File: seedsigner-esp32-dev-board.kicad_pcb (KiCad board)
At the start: 2 copper layers, 71.1 x 78.7 mm, 5 parts, among them J1 Conn_01x05, U1 ESP32-S2-SAOLA-1M, U2 OV_CAMERA, U3 RASPBERRY_PI_3_MODEL_B+

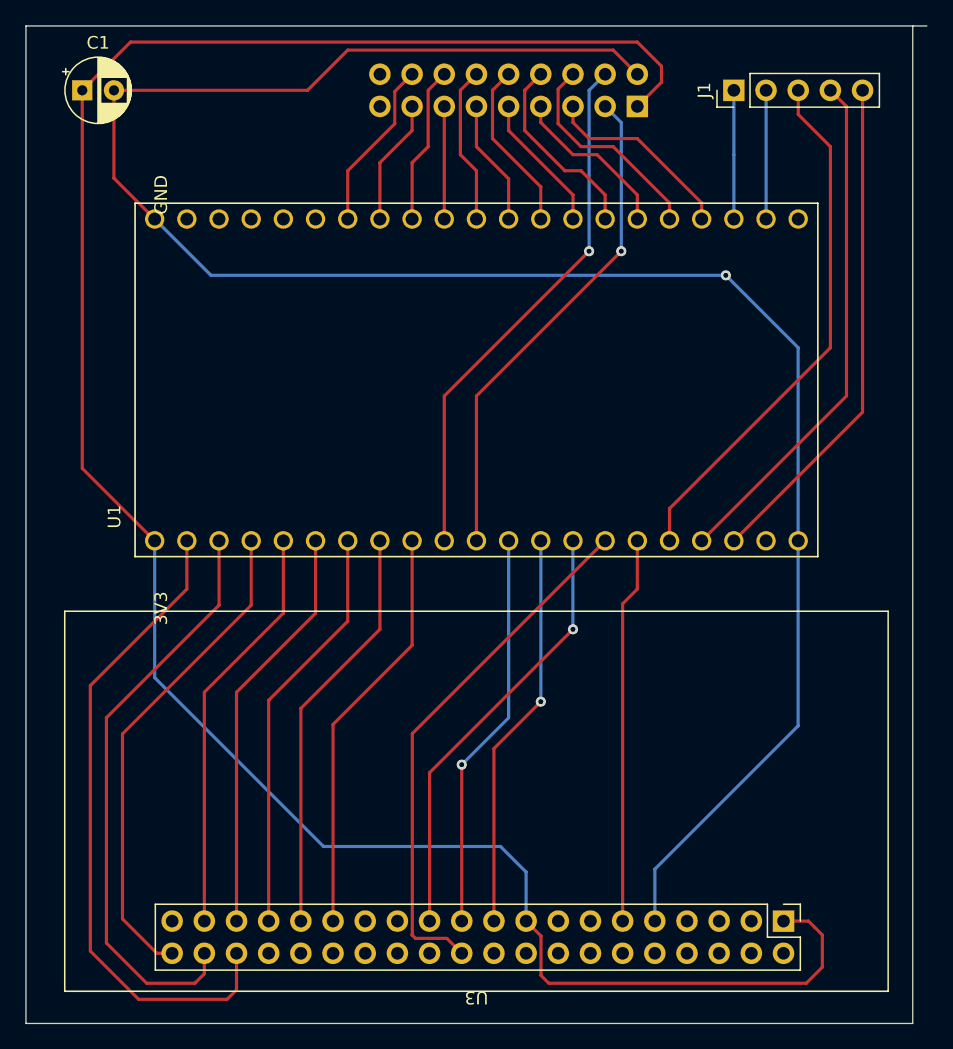
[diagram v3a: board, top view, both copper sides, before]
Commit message: fix small wiring issue, add mounting hole for lcd, add silkscreen
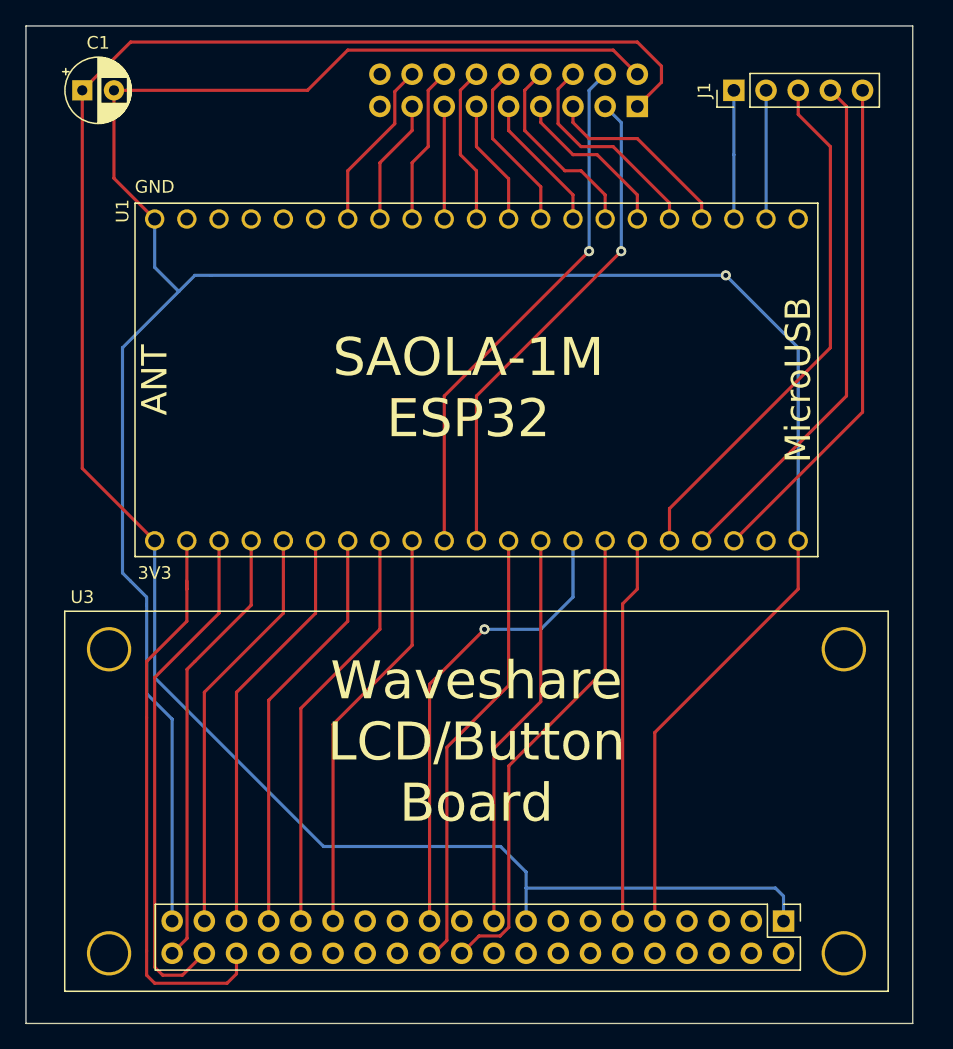
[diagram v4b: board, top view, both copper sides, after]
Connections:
- U3 pad 21: /SPI_CS -> unconnected-(U3-Pad21)
- U3 pad 24: unconnected-(U3-Pad24) -> /SPI_CS
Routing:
- net GND: track 159.9 -> 216.3 mm
- net +3.3V: track 174.1 -> 162.9 mm
- net /KEY3: track 51.9 -> 45.5 mm
- net /KEY2: track 46.4 -> 40.7 mm
- net /KEY1: track 39.1 -> 35.1 mm
- net /SPI_CS: track 31.6 -> 35.3 mm, vias 1 -> 0
- net /DC: track 41.9 -> 38.2 mm
- net /SPI_SCLK: track 34.7 -> 37.3 mm
- net /SPI_MOSI: vias 1 -> 0
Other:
- board size 71.1 x 78.7 mm -> 70 x 78.7 mm
- board text added: "ANT"
- board text added: "MicroUSB"
- board text added: "OV2640 Camera"
- board text added: "SAOLA-1M ESP32"
- board text added: "Waveshare LCD/Button Board"

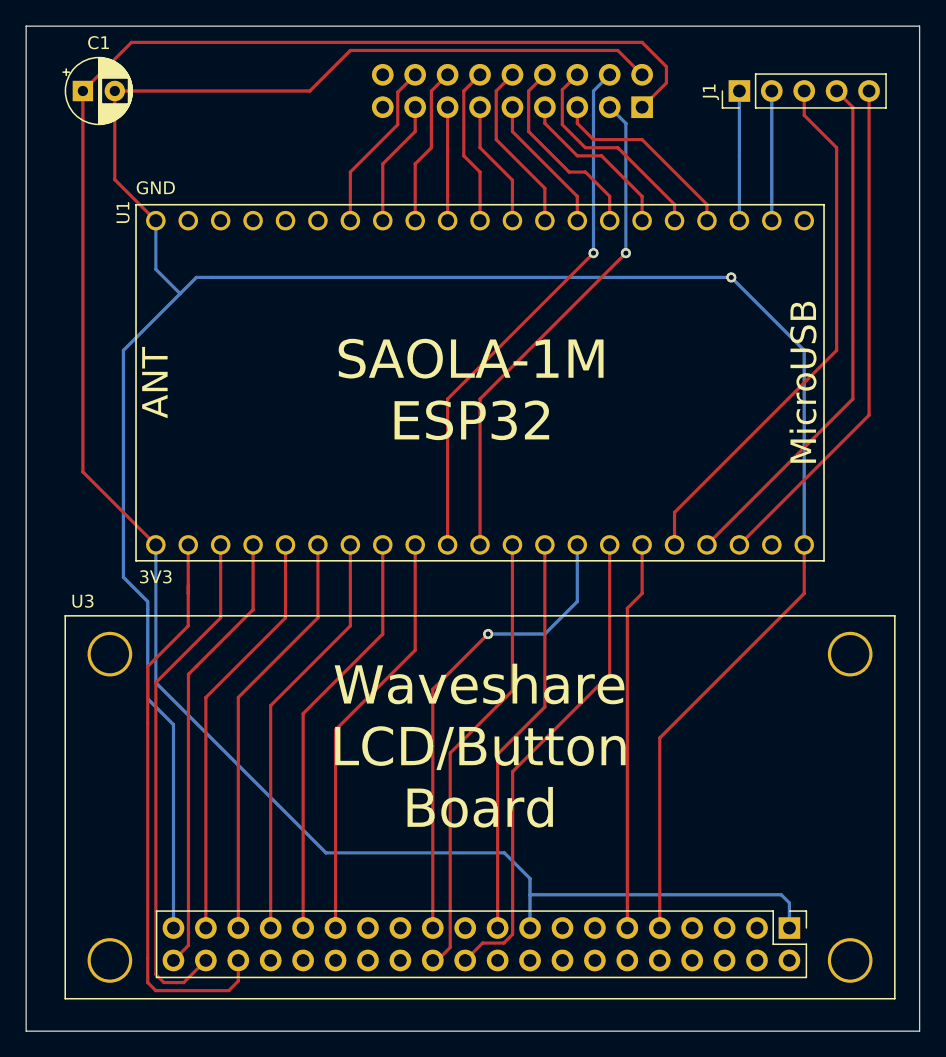
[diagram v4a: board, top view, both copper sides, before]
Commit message: add holes and seedsigner logo
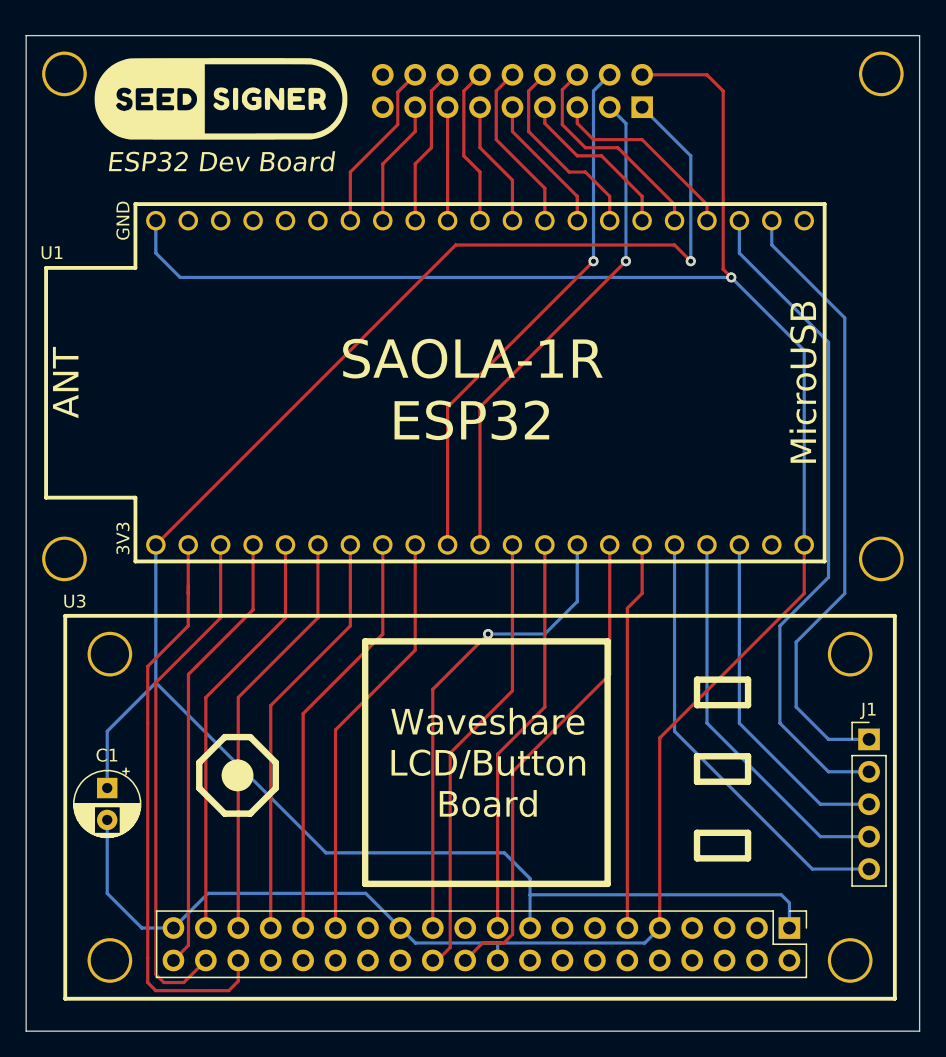
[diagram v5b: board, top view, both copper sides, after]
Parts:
- added H1: MountingHole, SeedSigner:MOUNT_HOLE_3MM, F.Cu at (67.0, -37.0)
- added H2: MountingHole, SeedSigner:MOUNT_HOLE_3MM, F.Cu at (3.00, -37.0)
- added H3: MountingHole, SeedSigner:MOUNT_HOLE_3MM, F.Cu at (67.0, -75.0)
- added H4: MountingHole, SeedSigner:MOUNT_HOLE_3MM, F.Cu at (3.00, -75.0)
- added LOGO1: SS_LOGO, SeedSigner:seedsigner-logo-small, F.Cu at (15.2, -73.0)
- moved C1 54.6 mm to (6.35, -19.1), turned to -90 degrees
- moved J1 51.8 mm to (66.0, -22.9), turned to 0 degrees
- moved U3 15.0 mm to (35.6, -17.5)
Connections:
- U1 pad 15: /XTRA3 -> /XTRA5
- U1 pad 17: /XTRA5 -> /XTRA3
- U1 pad 19: /XTRA2 -> /XTRA1
- U1 pad 20: /XTRA1 -> /XTRA2
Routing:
- net /XTRA2: track 10.2 -> 52.4 mm
- net /XTRA1: track 10.2 -> 48.8 mm
- net GND: track 216.3 -> 183.0 mm
- net /XTRA3: track 41.9 -> 26.8 mm
- net +3.3V: track 162.9 -> 148.5 mm, vias 0 -> 1
- net /XTRA4: track 40.8 -> 30.4 mm
- net /XTRA5: track 39.8 -> 34.3 mm
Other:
- board size 70 x 78.7 mm -> 70 x 78 mm
- board text added: "ESP32 Dev Board"
- board text added: "SAOLA-1R ESP32"
- board text removed: "SAOLA-1M ESP32"

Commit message: cleanup and add header for DE2120
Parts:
- added J2: Conn_01x08, Connector_PinSocket_2.00mm:PinSocket_1x08_P2.00mm_Vertical, B.Cu at (65.5, -24.2)
- J1: value Conn_01x05 -> Conn_01x06; footprint Connector_PinHeader_2.54mm:PinHeader_1x05_P2.54mm_Vertical -> Connector_PinHeader_2.54mm:PinHeader_1x06_P2.54mm_Vertical; moved to B.Cu
- moved J1 68.9 mm to (21.8, -75.7), turned to 90 degrees
- moved LOGO1 2.47 mm to (14.7, -70.6)
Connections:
- J1 pad 1: /XTRA1 -> GND
- J1 pad 2: /XTRA2 -> /TX
- J1 pad 3: /XTRA3 -> /RX
- J1 pad 4: /XTRA4 -> +3.3V
- J1 pad 5: /XTRA5 -> /IO_TRIG
- U1 pad 45: unconnected-(U1-Pad45) -> /IO_TRIG
- U1 pad 46: unconnected-(U1-Pad46) -> /IO_IN
- U1 pad RX: unconnected-(U1-PadRX) -> /RX
- U1 pad TX: unconnected-(U1-PadTX) -> /TX
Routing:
- net +3.3V: track 148.5 -> 181.1 mm
- net GND: track 183.0 -> 214.5 mm
- net +5V: track 0.00 -> 21.7 mm, vias 0 -> 1
- net /IO_TRIG: track 0.00 -> 14.7 mm
- net /IO_IN: track 0.00 -> 14.7 mm
- net /RX: track 0.00 -> 13.7 mm
- net /TX: track 0.00 -> 13.7 mm
- net /XTRA1: track 48.8 -> 50.5 mm
- net /XTRA4: track 30.4 -> 31.9 mm
- net /XTRA2: track 52.4 -> 53.9 mm
- net /XTRA5: track 34.3 -> 35.3 mm
- net /XTRA3: track 26.8 -> 27.6 mm
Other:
- board text added: "3.3V"
- board text added: "5V"
- board text added: "DE2120 Scanner"
- board text added: "Dev Board"
- board text added: "EXPANSION"
- board text added: "GND"
- board text added: "P15"
- board text added: "P16"
- board text added: "P17"
- board text added: "P19"
- board text added: "P20"
- board text added: "RX"
- board text added: "SAOLA-1R"
- board text added: "STAT"
- board text added: "TRIG"
- board text added: "TX"
- board text added: "Waveshare LCD HAT"
- board text removed: "ESP32 Dev Board"
- board text removed: "SAOLA-1R ESP32"
- board text removed: "Waveshare LCD/Button Board"

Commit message: small silkscreen adjustments
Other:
- board text added: "15"
- board text added: "16"
- board text added: "17"
- board text added: "19"
- board text added: "20"
- board text removed: "DE2120 Scanner"
- board text removed: "P15"
- board text removed: "P16"
- board text removed: "P17"
- board text removed: "P19"
- board text removed: "P20"
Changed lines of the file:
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@@
     (property "Sheetname" "")
     (attr through_hole)
-    (fp_text reference "J1" (at 0 2.54 90) (layer "B.SilkS")
+    (fp_text reference "J1" (at 0 -15.24 270) (layer "B.SilkS")
       (effects (font (size 1 1) (thickness 0.15)) (justify mirror))
     )
@@
     (property "Sheetname" "")
     (attr through_hole)
-    (fp_text reference "J2" (at 0 2.5) (layer "B.SilkS")
+    (fp_text reference "J2" (at 0 2.192) (layer "B.SilkS")
       (effects (font (size 1 1) (thickness 0.15)) (justify mirror))
     )
@@
   (gr_line (start 0 -78) (end 0 0) (layer "Edge.Cuts") (width 0.1))
   (gr_line (start 70 0) (end 70 -78) (layer "Edge.Cuts") (width 0.1))
-  (gr_text "RX" (at 16.764 -73.66) (layer "B.SilkS")
-    (effects (font (size 0.7 0.7) (thickness 0.125)) (justify mirror))
-  )
-  (gr_text "3.3V" (at 67.31 -9.144 90) (layer "B.SilkS")
+  (gr_text "RX" (at 16.764 -73.406 270) (layer "B.SilkS")
+    (effects (font (size 0.7 0.7) (thickness 0.125)) (justify mirror))
+  )
+  (gr_text "3.3V" (at 68.072 -10.16) (layer "B.SilkS")
     (effects (font (size 0.7 0.7) (thickness 0.125)) (justify mirror))
   )
@@
     (effects (font (size 1.5 1.5) (thickness 0.3)) (justify mirror))
   )
-  (gr_text "GND" (at 67.31 -24.638 90) (layer "B.SilkS")
-    (effects (font (size 0.7 0.7) (thickness 0.125)) (justify mirror))
-  )
-  (gr_text "P16" (at 67.31 -13.97 90) (layer "B.SilkS")
+  (gr_text "GND" (at 67.818 -24.13) (layer "B.SilkS")
+    (effects (font (size 0.7 0.7) (thickness 0.125)) (justify mirror))
+  )
+  (gr_text "16" (at 67.564 -13.97) (layer "B.SilkS")
     (effects (font (size 0.7 0.7) (thickness 0.125)) (justify mirror))
   )
@@
     (effects (font (size 2 2) (thickness 0.3)) (justify mirror))
   )
-  (gr_text "GND" (at 21.844 -73.66) (layer "B.SilkS")
-    (effects (font (size 0.7 0.7) (thickness 0.125)) (justify mirror))
-  )
-  (gr_text "P19" (at 67.31 -20.828 90) (layer "B.SilkS")
-    (effects (font (size 0.7 0.7) (thickness 0.125)) (justify mirror))
-  )
-  (gr_text "STAT" (at 8.89 -73.66) (layer "B.SilkS")
-    (effects (font (size 0.7 0.7) (thickness 0.125)) (justify mirror))
-  )
-  (gr_text "5V" (at 67.31 -22.606 90) (layer "B.SilkS")
-    (effects (font (size 0.7 0.7) (thickness 0.125)) (justify mirror))
-  )
-  (gr_text "DE2120\nScanner" (at 15.24 -70.104) (layer "B.SilkS")
-    (effects (font (size 2 2) (thickness 0.3)) (justify mirror))
-  )
-  (gr_text "P17" (at 67.31 -16.256 90) (layer "B.SilkS")
-    (effects (font (size 0.7 0.7) (thickness 0.125)) (justify mirror))
-  )
-  (gr_text "P20" (at 67.31 -18.542 90) (layer "B.SilkS")
-    (effects (font (size 0.7 0.7) (thickness 0.125)) (justify mirror))
-  )
-  (gr_text "3.3V" (at 14.478 -73.66) (layer "B.SilkS")
-    (effects (font (size 0.7 0.7) (thickness 0.125)) (justify mirror))
-  )
-  (gr_text "TRIG" (at 11.684 -73.66) (layer "B.SilkS")
-    (effects (font (size 0.7 0.7) (thickness 0.125)) (justify mirror))
-  )
-  (gr_text "P15" (at 67.31 -11.684 90) (layer "B.SilkS")
-    (effects (font (size 0.7 0.7) (thickness 0.125)) (justify mirror))
-  )
-  (gr_text "TX" (at 19.304 -73.66) (layer "B.SilkS")
-    (effects (font (size 0.7 0.7) (thickness 0.125)) (justify mirror))
-  )
+  (gr_text "EXPANSION" (at 14.732 -70.612) (layer "B.SilkS")
+    (effects (font (size 1.5 1.5) (thickness 0.3)) (justify mirror))
+  )
+  (gr_text "GND" (at 21.844 -72.898 270) (layer "B.SilkS")
+    (effects (font (size 0.7 0.7) (thickness 0.125)) (justify mirror))
+  )
+  (gr_text "19" (at 67.564 -20.32) (layer "B.SilkS")
+    (effects (font (size 0.7 0.7) (thickness 0.125)) (justify mirror))
+  )
+  (gr_text "STAT" (at 9.144 -72.898 270) (layer "B.SilkS")
+    (effects (font (size 0.7 0.7) (thickness 0.125)) (justify mirror))
+  )
+  (gr_text "5V" (at 67.564 -22.098) (layer "B.SilkS")
+    (effects (font (size 0.7 0.7) (thickness 0.125)) (justify mirror))
+  )
+  (gr_text "17" (at 67.564 -16.256 90) (layer "B.SilkS")
+    (effects (font (size 0.7 0.7) (thickness 0.125)) (justify mirror))
+  )
+  (gr_text "20" (at 67.564 -18.542) (layer "B.SilkS")
+    (effects (font (size 0.7 0.7) (thickness 0.125)) (justify mirror))
+  )
+  (gr_text "3.3V" (at 14.224 -72.898 270) (layer "B.SilkS")
+    (effects (font (size 0.7 0.7) (thickness 0.125)) (justify mirror))
+  )
+  (gr_text "TRIG" (at 11.684 -72.898 270) (layer "B.SilkS")
+    (effects (font (size 0.7 0.7) (thickness 0.125)) (justify mirror))
+  )
+  (gr_text "15" (at 67.564 -12.192) (layer "B.SilkS")
+    (effects (font (size 0.7 0.7) (thickness 0.125)) (justify mirror))
+  )
+  (gr_text "TX" (at 19.304 -73.406 270) (layer "B.SilkS")
+    (effects (font (size 0.7 0.7) (thickness 0.125)) (justify mirror))
+  )
